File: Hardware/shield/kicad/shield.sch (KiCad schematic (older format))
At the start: 25 parts, among them P101 anemo1, P102 anemo2, P103 vane, P104 AC_in, P105 DC_in, P106 current1, P107 current2, P108 current3, P109 current4, P110 temp, P111 RPM, P112 Power, P113 Analog, P114 5VDC, P115 POWER_SOURCE, P116 PWM, P117 PWM, P118 Communication, P119 h1, P120 h2, P121 h3, P122 h4

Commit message: add shield_preview.jpg
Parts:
- removed P119: h1, Socket_Arduino_Mega:Arduino_1pin, symbol CONN_01X01
- added P123: h5, Socket_Arduino_Mega:Arduino_1pin, symbol CONN_01X01
- added P124: h6, Socket_Arduino_Mega:Arduino_1pin, symbol CONN_01X01
- added P125: h7, Socket_Arduino_Mega:Arduino_1pin, symbol CONN_01X01
- added P126: h8, Socket_Arduino_Mega:Arduino_1pin, symbol CONN_01X01
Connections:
- no-connect marks 31 -> 34
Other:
- note added: "Fixation Holes"
- moved on the sheet: P120, P121, P122
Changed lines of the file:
@@
-$EndComp
-$Comp
-L CONN_01X01 P119
-U 1 1 5803A06D
-P 7675 5875
-F 0 "P119" H 7950 5875 50  0000 C CNN
-F 1 "h1" H 7775 5875 50  0000 C CNN
-F 2 "Socket_Arduino_Mega:Arduino_1pin" H 7675 5875 50  0001 C CNN
-F 3 "" H 7675 5875 50  0000 C CNN
-	1    7675 5875
-	1    0    0    -1
 $EndComp
 $Comp
 L CONN_01X01 P120
 U 1 1 5803AC24
-P 7675 6000
-F 0 "P120" H 7950 6000 50  0000 C CNN
-F 1 "h2" H 7775 6000 50  0000 C CNN
-F 2 "Socket_Arduino_Mega:Arduino_1pin" H 7675 6000 50  0001 C CNN
-F 3 "" H 7675 6000 50  0000 C CNN
-	1    7675 6000
+P 7300 6050
+F 0 "P120" H 7575 6050 50  0000 C CNN
+F 1 "h2" H 7400 6050 50  0000 C CNN
+F 2 "Socket_Arduino_Mega:Arduino_1pin" H 7300 6050 50  0001 C CNN
+F 3 "" H 7300 6050 50  0000 C CNN
+	1    7300 6050
 	1    0    0    -1
 $EndComp
@@
 L CONN_01X01 P121
 U 1 1 5803AD27
-P 7675 6125
-F 0 "P121" H 7950 6125 50  0000 C CNN
-F 1 "h3" H 7775 6125 50  0000 C CNN
-F 2 "Socket_Arduino_Mega:Arduino_1pin" H 7675 6125 50  0001 C CNN
-F 3 "" H 7675 6125 50  0000 C CNN
-	1    7675 6125
+P 7300 6175
+F 0 "P121" H 7575 6175 50  0000 C CNN
+F 1 "h3" H 7400 6175 50  0000 C CNN
+F 2 "Socket_Arduino_Mega:Arduino_1pin" H 7300 6175 50  0001 C CNN
+F 3 "" H 7300 6175 50  0000 C CNN
+	1    7300 6175
 	1    0    0    -1
 $EndComp
@@
 L CONN_01X01 P122
 U 1 1 5803AE2D
-P 7675 6250
-F 0 "P122" H 7950 6250 50  0000 C CNN
-F 1 "h4" H 7775 6250 50  0000 C CNN
-F 2 "Socket_Arduino_Mega:Arduino_1pin" H 7675 6250 50  0001 C CNN
-F 3 "" H 7675 6250 50  0000 C CNN
-	1    7675 6250
+P 7300 6300
+F 0 "P122" H 7575 6300 50  0000 C CNN
+F 1 "h4" H 7400 6300 50  0000 C CNN
+F 2 "Socket_Arduino_Mega:Arduino_1pin" H 7300 6300 50  0001 C CNN
+F 3 "" H 7300 6300 50  0000 C CNN
+	1    7300 6300
 	1    0    0    -1
 $EndComp
-NoConn ~ 7475 5875
-NoConn ~ 7475 6000
-NoConn ~ 7475 6125
-NoConn ~ 7475 6250
+NoConn ~ 7100 6050
+NoConn ~ 7100 6175
+NoConn ~ 7100 6300
+$Comp
+L CONN_01X01 P123
+U 1 1 5803B1D2
+P 8075 5925
+F 0 "P123" H 8350 5925 50  0000 C CNN
+F 1 "h5" H 8175 5925 50  0000 C CNN
+F 2 "Socket_Arduino_Mega:Arduino_1pin" H 8075 5925 50  0001 C CNN
+F 3 "" H 8075 5925 50  0000 C CNN
+	1    8075 5925
+	1    0    0    -1
+$EndComp
+$Comp
+L CONN_01X01 P124
+U 1 1 5803B1D8
+P 8075 6050
+F 0 "P124" H 8350 6050 50  0000 C CNN
+F 1 "h6" H 8175 6050 50  0000 C CNN
+F 2 "Socket_Arduino_Mega:Arduino_1pin" H 8075 6050 50  0001 C CNN
+F 3 "" H 8075 6050 50  0000 C CNN
+	1    8075 6050
+	1    0    0    -1
+$EndComp
+$Comp
+L CONN_01X01 P125
+U 1 1 5803B1DE
+P 8075 6175
+F 0 "P125" H 8350 6175 50  0000 C CNN
+F 1 "h7" H 8175 6175 50  0000 C CNN
+F 2 "Socket_Arduino_Mega:Arduino_1pin" H 8075 6175 50  0001 C CNN
+F 3 "" H 8075 6175 50  0000 C CNN
+	1    8075 6175
+	1    0    0    -1
+$EndComp
+$Comp
+L CONN_01X01 P126
+U 1 1 5803B1E4
+P 8075 6300
+F 0 "P126" H 8350 6300 50  0000 C CNN
+F 1 "h8" H 8175 6300 50  0000 C CNN
+F 2 "Socket_Arduino_Mega:Arduino_1pin" H 8075 6300 50  0001 C CNN
+F 3 "" H 8075 6300 50  0000 C CNN
+	1    8075 6300
+	1    0    0    -1
+$EndComp
+NoConn ~ 7875 5925
+NoConn ~ 7875 6050
+NoConn ~ 7875 6175
+NoConn ~ 7875 6300
+Text Notes 7425 5825 0    60   ~ 0
+Fixation Holes
 $EndSCHEMATC

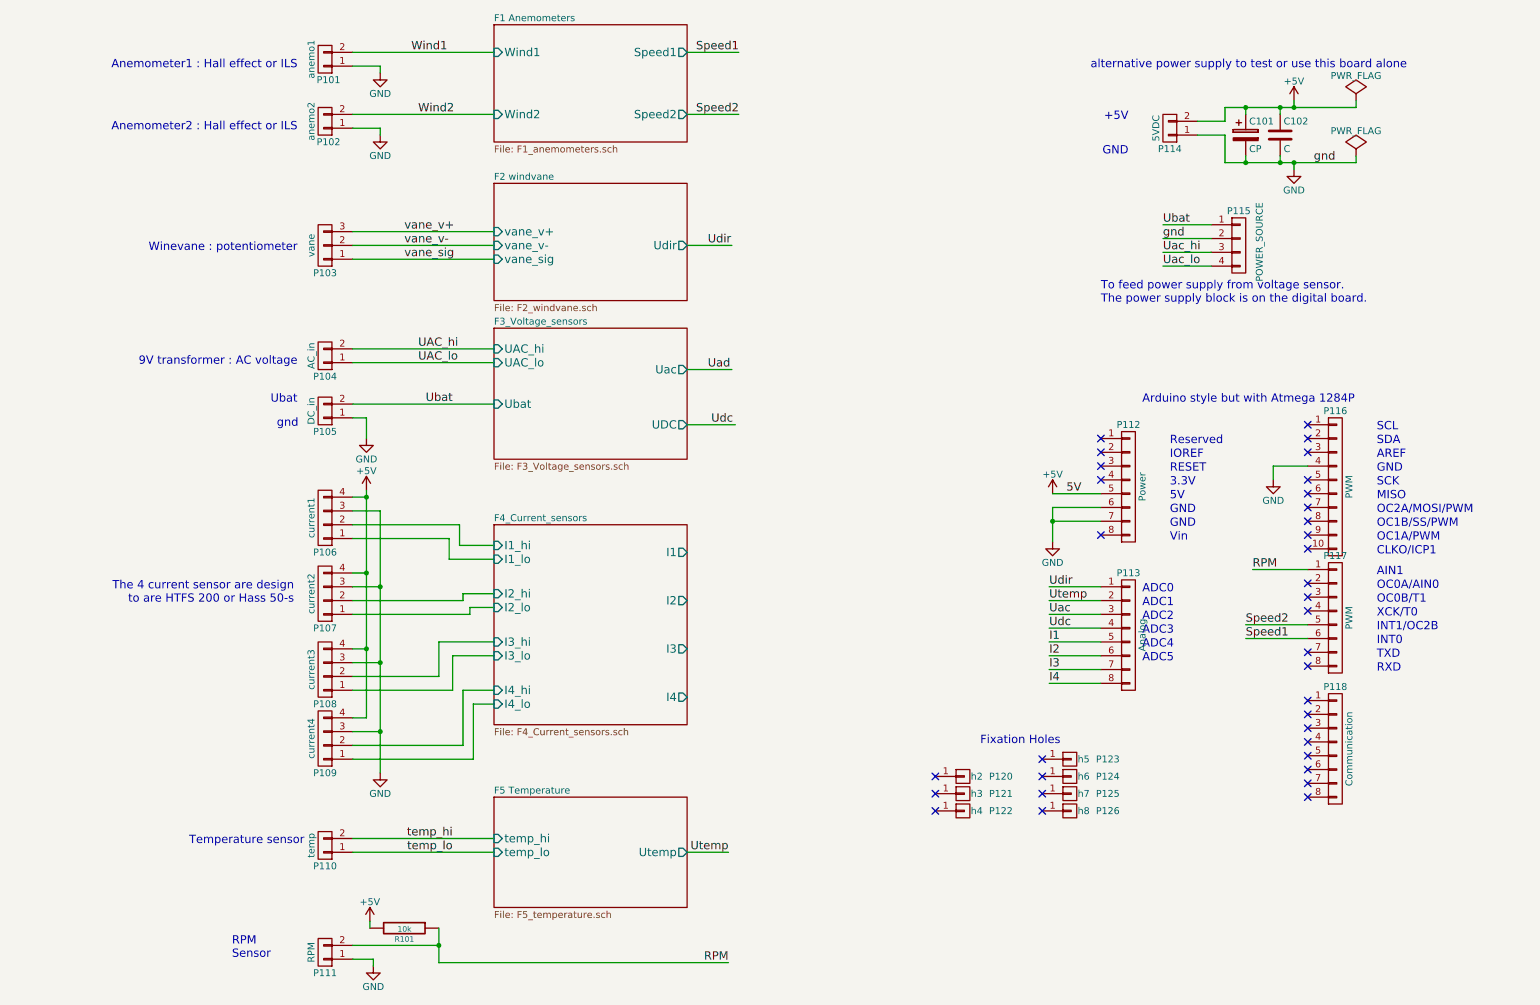
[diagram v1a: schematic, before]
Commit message: Update shield to 2.0.0
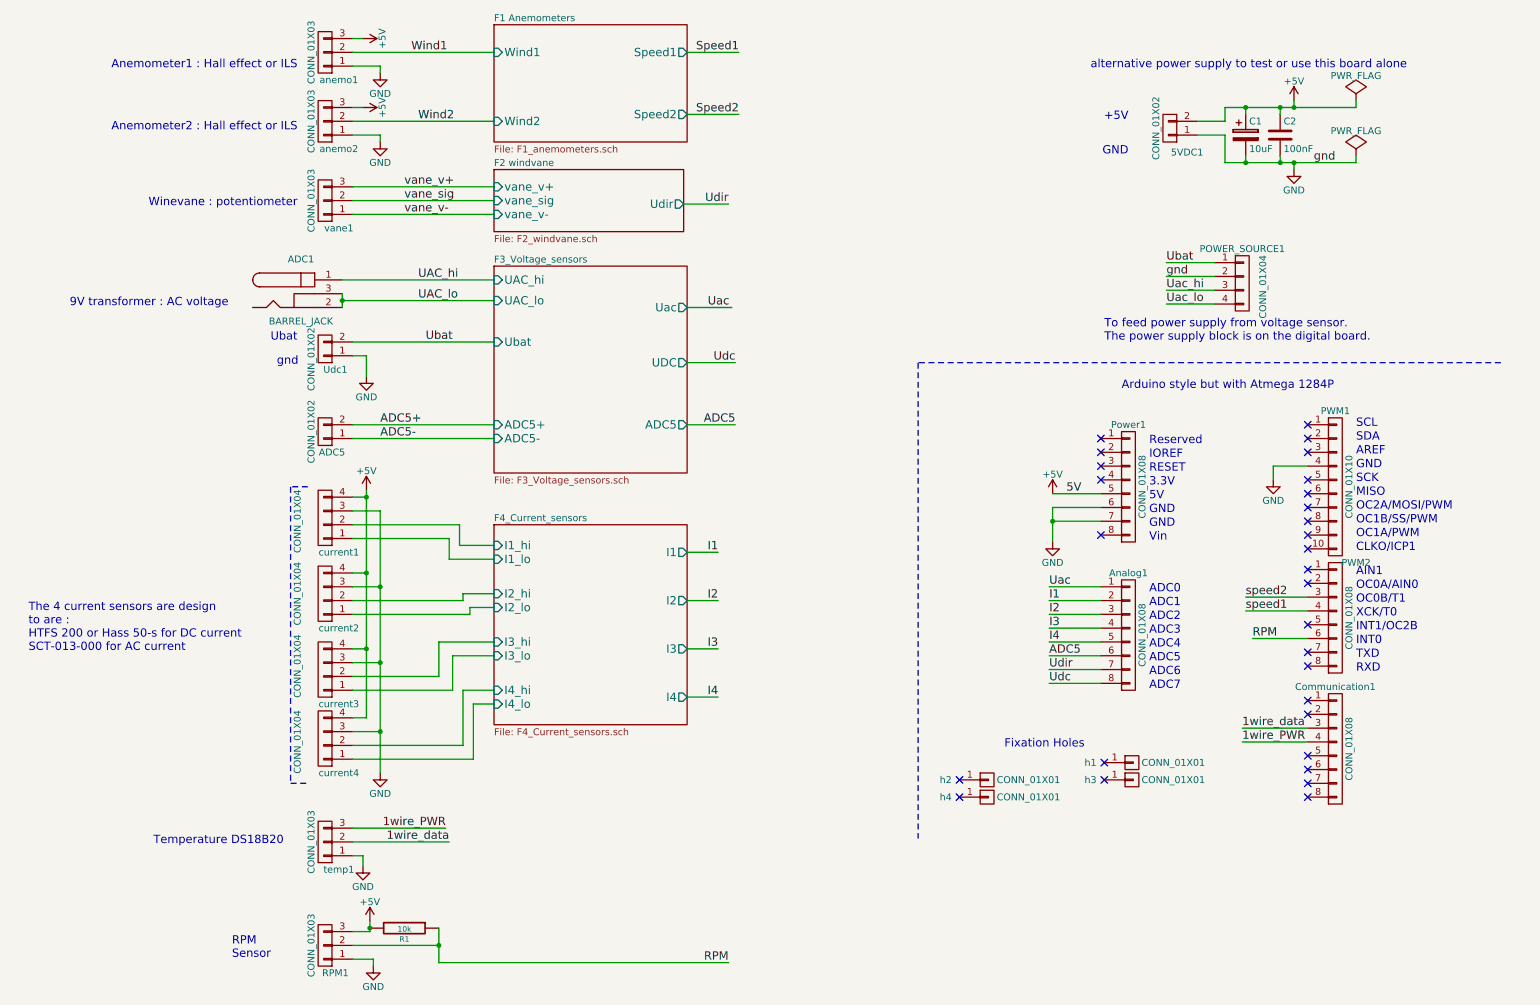
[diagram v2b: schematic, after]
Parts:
- removed P101: anemo1, Terminal_Blocks:TerminalBlock_Pheonix_MKDS1.5-2pol, symbol CONN_01X02
- removed P102: anemo2, Terminal_Blocks:TerminalBlock_Pheonix_MKDS1.5-2pol, symbol CONN_01X02
- removed P103: vane, Terminal_Blocks:TerminalBlock_Pheonix_MKDS1.5-3pol, symbol CONN_01X03
- removed P104: AC_in, Terminal_Blocks:TerminalBlock_Pheonix_MKDS1.5-2pol, symbol CONN_01X02
- removed P105: DC_in, Terminal_Blocks:TerminalBlock_Pheonix_MKDS1.5-2pol, symbol CONN_01X02
- removed P106: current1, Terminal_Blocks:TerminalBlock_Pheonix_MKDS1.5-4pol, symbol CONN_01X04
- removed P107: current2, Terminal_Blocks:TerminalBlock_Pheonix_MKDS1.5-4pol, symbol CONN_01X04
- removed P108: current3, Terminal_Blocks:TerminalBlock_Pheonix_MKDS1.5-4pol, symbol CONN_01X04
- removed P109: current4, Terminal_Blocks:TerminalBlock_Pheonix_MKDS1.5-4pol, symbol CONN_01X04
- removed P110: temp, Terminal_Blocks:TerminalBlock_Pheonix_MKDS1.5-2pol, symbol CONN_01X02
- removed P111: RPM, Terminal_Blocks:TerminalBlock_Pheonix_MKDS1.5-2pol, symbol CONN_01X02
- removed P112: Power, Socket_Arduino_Mega:Socket_Strip_Arduino_1x08, symbol CONN_01X08
- removed P113: Analog, Socket_Arduino_Mega:Socket_Strip_Arduino_1x08, symbol CONN_01X08
- removed P114: 5VDC, Socket_Strips:Socket_Strip_Straight_1x02, symbol CONN_01X02
- removed P115: POWER_SOURCE, Socket_Strips:Socket_Strip_Straight_1x04, symbol CONN_01X04
- removed P116: PWM, Socket_Arduino_Mega:Socket_Strip_Arduino_1x10, symbol CONN_01X10
- removed P117: PWM, Socket_Arduino_Mega:Socket_Strip_Arduino_1x08, symbol CONN_01X08
- removed P118: Communication, Socket_Arduino_Mega:Socket_Strip_Arduino_1x08, symbol CONN_01X08
- removed P120: h2, Socket_Arduino_Mega:Arduino_1pin, symbol CONN_01X01
- removed P121: h3, Socket_Arduino_Mega:Arduino_1pin, symbol CONN_01X01
- removed P122: h4, Socket_Arduino_Mega:Arduino_1pin, symbol CONN_01X01
- removed P123: h5, Socket_Arduino_Mega:Arduino_1pin, symbol CONN_01X01
- removed P124: h6, Socket_Arduino_Mega:Arduino_1pin, symbol CONN_01X01
- removed P125: h7, Socket_Arduino_Mega:Arduino_1pin, symbol CONN_01X01
- removed P126: h8, Socket_Arduino_Mega:Arduino_1pin, symbol CONN_01X01
- added 5VDC1: CONN_01X02, Socket_Strips:Socket_Strip_Straight_1x02, symbol CONN_01X02
- added ADC1: BARREL_JACK, Connect:BARREL_JACK, symbol BARREL_JACK
- added ADC5, Udc1: CONN_01X02, w_conn_screw:mstba_2,5%2f2-g-5,08, symbol CONN_01X02
- added Analog1, Communication1, PWM2, Power1: CONN_01X08, Socket_Arduino_Mega:Socket_Strip_Arduino_1x08, symbol CONN_01X08
- added POWER_SOURCE1: CONN_01X04, Socket_Strips:Socket_Strip_Straight_1x04, symbol CONN_01X04
- added PWM1: CONN_01X10, Socket_Arduino_Mega:Socket_Strip_Arduino_1x10, symbol CONN_01X10
- added RPM1, anemo1, anemo2, temp1, vane1: CONN_01X03, w_conn_screw:mstba_2,5%2f3-g-5,08, symbol CONN_01X03
- added current1, current2, current3, current4: CONN_01X04, w_conn_screw:mstba_2,5%2f4-g-5,08, symbol CONN_01X04
- added h1, h2, h3, h4: CONN_01X01, Socket_Arduino_Mega:Arduino_1pin, symbol CONN_01X01
- C1: renamed from C101; value CP -> 10uF
- C2: renamed from C102; value C -> 100nF; footprint Capacitors_ThroughHole:C_Radial_D5_L6_P2.5 -> Capacitors_ThroughHole:C_Rect_L7_W2.5_P5
- R1: renamed from R101; footprint Discret:R4 -> Discret:R3-LARGE_PADS
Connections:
- net +5V: now also 5VDC1.2 (P2), Power1.5 (P5), RPM1.3 (P3), anemo1.3 (P3), anemo2.3 (P3), current1.4 (P4), current2.4 (P4), current3.4 (P4), current4.4 (P4)
- net F4_Current_sensors/I1_hi: now also current1.2 (P2)
- net F4_Current_sensors/I1_lo: now also current1.1 (P1)
- net F4_Current_sensors/I2_hi: now also current2.2 (P2)
- net F4_Current_sensors/I2_lo: now also current2.1 (P1)
- net F4_Current_sensors/I3_hi: now also current3.2 (P2)
- net F4_Current_sensors/I3_lo: now also current3.1 (P1)
- net F4_Current_sensors/I4_hi: now also current4.2 (P2)
- net F4_Current_sensors/I4_lo: now also current4.1 (P1)
- net GND: now also 5VDC1.1 (P1), POWER_SOURCE1.2 (P2), PWM1.4 (P4), Power1.6 (P6), Power1.7 (P7), RPM1.1 (P1), Udc1.1 (P1), anemo1.1 (P1), anemo2.1 (P1), current1.3 (P3), current2.3 (P3), current3.3 (P3), current4.3 (P3), temp1.1 (P1)
- net I1: now also Analog1.2 (P2)
- net I2: now also Analog1.3 (P3)
- net I3: now also Analog1.4 (P4)
- net I4: now also Analog1.5 (P5)
- net RPM: now also PWM2.6 (P6), RPM1.2 (P2)
- net UAC_hi: now also ADC1.1
- net UAC_lo: now also ADC1.2, ADC1.3
- net Uac: now also Analog1.1 (P1)
- net Uac_hi: now also POWER_SOURCE1.3 (P3)
- net Uac_lo: now also POWER_SOURCE1.4 (P4)
- net Ubat: now also POWER_SOURCE1.1 (P1), Udc1.2 (P2)
- net Udc: now also Analog1.8 (P8)
- net Udir: now also Analog1.7 (P7)
- net Wind1: now also anemo1.2 (P2)
- net Wind2: now also anemo2.2 (P2)
- net vane_sig: now also vane1.2 (P2)
- net vane_v+: now also vane1.3 (P3)
- net vane_v-: now also vane1.1 (P1)
- new net 1wire_PWR: Communication1.4 (P4), temp1.3 (P3)
- new net 1wire_data: Communication1.3 (P3), temp1.2 (P2)
- new net ADC5: Analog1.6 (P6)
- new net ADC5+: ADC5.2 (P2)
- new net ADC5-: ADC5.1 (P1)
- new net speed1: PWM2.4 (P4)
- new net speed2: PWM2.3 (P3)
- no-connect marks 34 -> 29
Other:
- note added: "ADC6"
- note added: "ADC7"
- note added: "Temperature DS18B20"
- note added: "The 4 current sensors are design \nto are :\nHTFS 200 or Hass 50-s for DC current\nSCT-013-000 for AC current"
- note removed: "Temperature sensor"
- note removed: "The 4 current sensor are design \nto are HTFS 200 or Hass 50-s"

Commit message: move to digital 1.1.1
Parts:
- removed 5VDC1: CONN_01X02, Socket_Strips:Socket_Strip_Straight_1x02, symbol CONN_01X02
- removed ADC1: BARREL_JACK, Connect:BARREL_JACK, symbol BARREL_JACK
- removed ADC5, Udc1: CONN_01X02, w_conn_screw:mstba_2,5%2f2-g-5,08, symbol CONN_01X02
- removed Analog1, Communication1, PWM2, Power1: CONN_01X08, Socket_Arduino_Mega:Socket_Strip_Arduino_1x08, symbol CONN_01X08
- removed POWER_SOURCE1: CONN_01X04, Socket_Strips:Socket_Strip_Straight_1x04, symbol CONN_01X04
- removed PWM1: CONN_01X10, Socket_Arduino_Mega:Socket_Strip_Arduino_1x10, symbol CONN_01X10
- removed RPM1, anemo1, anemo2, temp1, vane1: CONN_01X03, w_conn_screw:mstba_2,5%2f3-g-5,08, symbol CONN_01X03
- removed current1, current2, current3, current4: CONN_01X04, w_conn_screw:mstba_2,5%2f4-g-5,08, symbol CONN_01X04
- removed h1, h2, h3, h4: CONN_01X01, Socket_Arduino_Mega:Arduino_1pin, symbol CONN_01X01
- added P101: anemo1, Terminal_Blocks:TerminalBlock_Pheonix_MKDS1.5-2pol, symbol CONN_01X02
- added P102: anemo2, Terminal_Blocks:TerminalBlock_Pheonix_MKDS1.5-2pol, symbol CONN_01X02
- added P103: vane, Terminal_Blocks:TerminalBlock_Pheonix_MKDS1.5-3pol, symbol CONN_01X03
- added P104: AC_in, Terminal_Blocks:TerminalBlock_Pheonix_MKDS1.5-2pol, symbol CONN_01X02
- added P105: DC_in, Terminal_Blocks:TerminalBlock_Pheonix_MKDS1.5-2pol, symbol CONN_01X02
- added P106: current1, Terminal_Blocks:TerminalBlock_Pheonix_MKDS1.5-4pol, symbol CONN_01X04
- added P107: current2, Terminal_Blocks:TerminalBlock_Pheonix_MKDS1.5-4pol, symbol CONN_01X04
- added P108: current3, Terminal_Blocks:TerminalBlock_Pheonix_MKDS1.5-4pol, symbol CONN_01X04
- added P109: current4, Terminal_Blocks:TerminalBlock_Pheonix_MKDS1.5-4pol, symbol CONN_01X04
- added P110: temp, Terminal_Blocks:TerminalBlock_Pheonix_MKDS1.5-2pol, symbol CONN_01X02
- added P111: RPM, Terminal_Blocks:TerminalBlock_Pheonix_MKDS1.5-2pol, symbol CONN_01X02
- added P112: Power, Socket_Arduino_Mega:Socket_Strip_Arduino_1x08, symbol CONN_01X08
- added P113: Analog, Socket_Arduino_Mega:Socket_Strip_Arduino_1x08, symbol CONN_01X08
- added P114: 5VDC, Socket_Strips:Socket_Strip_Straight_1x02, symbol CONN_01X02
- added P115: POWER_SOURCE, Socket_Strips:Socket_Strip_Straight_1x04, symbol CONN_01X04
- added P116: PWM, Socket_Arduino_Mega:Socket_Strip_Arduino_1x10, symbol CONN_01X10
- added P117: PWM, Socket_Arduino_Mega:Socket_Strip_Arduino_1x08, symbol CONN_01X08
- added P118: Communication, Socket_Arduino_Mega:Socket_Strip_Arduino_1x08, symbol CONN_01X08
- added P120: h2, Socket_Arduino_Mega:Arduino_1pin, symbol CONN_01X01
- added P121: h3, Socket_Arduino_Mega:Arduino_1pin, symbol CONN_01X01
- added P122: h4, Socket_Arduino_Mega:Arduino_1pin, symbol CONN_01X01
- added P123: h5, Socket_Arduino_Mega:Arduino_1pin, symbol CONN_01X01
- added P124: h6, Socket_Arduino_Mega:Arduino_1pin, symbol CONN_01X01
- added P125: h7, Socket_Arduino_Mega:Arduino_1pin, symbol CONN_01X01
- added P126: h8, Socket_Arduino_Mega:Arduino_1pin, symbol CONN_01X01
- C101: renamed from C1; value 10uF -> CP
- C102: renamed from C2; value 100nF -> C; footprint Capacitors_ThroughHole:C_Rect_L7_W2.5_P5 -> Capacitors_ThroughHole:C_Radial_D5_L6_P2.5
- R101: renamed from R1; footprint Discret:R3-LARGE_PADS -> Discret:R4
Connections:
- net +5V: now also P106.4 (P4), P107.4 (P4), P108.4 (P4), P109.4 (P4), P112.5 (P5), P114.2 (P2)
- net F4_Current_sensors/I1_hi: now also P106.2 (P2)
- net F4_Current_sensors/I1_lo: now also P106.1 (P1)
- net F4_Current_sensors/I2_hi: now also P107.2 (P2)
- net F4_Current_sensors/I2_lo: now also P107.1 (P1)
- net F4_Current_sensors/I3_hi: now also P108.2 (P2)
- net F4_Current_sensors/I3_lo: now also P108.1 (P1)
- net F4_Current_sensors/I4_hi: now also P109.2 (P2)
- net F4_Current_sensors/I4_lo: now also P109.1 (P1)
- net GND: now also P101.1 (P1), P102.1 (P1), P105.1 (P1), P106.3 (P3), P107.3 (P3), P108.3 (P3), P109.3 (P3), P111.1 (P1), P112.6 (P6), P112.7 (P7), P114.1 (P1), P115.2 (P2), P116.4 (P4)
- net I1: now also P113.5 (P5)
- net I2: now also P113.6 (P6)
- net I3: now also P113.7 (P7)
- net I4: now also P113.8 (P8)
- net RPM: now also P111.2 (P2), P117.1 (P1)
- net Speed1: now also P117.6 (P6)
- net Speed2: now also P117.5 (P5)
- net UAC_hi: now also P104.2 (P2)
- net UAC_lo: now also P104.1 (P1)
- net Uac: now also P113.3 (P3)
- net Uac_hi: now also P115.3 (P3)
- net Uac_lo: now also P115.4 (P4)
- net Ubat: now also P105.2 (P2), P115.1 (P1)
- net Udc: now also P113.4 (P4)
- net Udir: now also P113.1 (P1)
- net Wind1: now also P101.2 (P2)
- net Wind2: now also P102.2 (P2)
- net vane_sig: now also P103.1 (P1)
- net vane_v+: now also P103.3 (P3)
- net vane_v-: now also P103.2 (P2)
- new net Utemp: P113.2 (P2)
- new net temp_hi: P110.2 (P2)
- new net temp_lo: P110.1 (P1)
- no-connect marks 29 -> 34
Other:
- note added: "Temperature sensor"
- note added: "The 4 current sensor are design \nto are HTFS 200 or Hass 50-s"
- note removed: "ADC6"
- note removed: "ADC7"
- note removed: "Temperature DS18B20"
- note removed: "The 4 current sensors are design \nto are :\nHTFS 200 or Hass 50-s for DC current\nSCT-013-000 for AC current"
